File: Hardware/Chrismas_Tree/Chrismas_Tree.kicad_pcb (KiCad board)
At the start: 2 copper layers, 144 parts

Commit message: Added tree trunk to schematic and PCB.
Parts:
- added D73: LED, LED_THT:LED_D5.0mm, F.Cu at (185.7, 325.6)
- added D74: LED, LED_THT:LED_D5.0mm, F.Cu at (136.7, 325.6)
- added D75: LED, LED_THT:LED_D5.0mm, F.Cu at (185.7, 337.6)
- added D76: LED, LED_THT:LED_D5.0mm, F.Cu at (136.7, 337.6)
- added D77: LED, LED_THT:LED_D5.0mm, F.Cu at (185.7, 348.7)
- added D78: LED, LED_THT:LED_D5.0mm, F.Cu at (136.7, 348.7)
- added D79: LED, LED_THT:LED_D5.0mm, F.Cu at (172.7, 350.0)
- added D80: LED, LED_THT:LED_D5.0mm, F.Cu at (149.9, 350.0)
- added D81: LED, LED_THT:LED_D5.0mm, F.Cu at (161.0, 350.0)
- added R73: R, Resistor_THT:R_Axial_DIN0207_L6.3mm_D2.5mm_P7.62mm_Horizontal, F.Cu at (429.0, 207.3)
- added R74: R, Resistor_THT:R_Axial_DIN0207_L6.3mm_D2.5mm_P7.62mm_Horizontal, F.Cu at (429.0, 211.4)
- added R75: R, Resistor_THT:R_Axial_DIN0207_L6.3mm_D2.5mm_P7.62mm_Horizontal, F.Cu at (439.8, 207.3)
- added R76: R, Resistor_THT:R_Axial_DIN0207_L6.3mm_D2.5mm_P7.62mm_Horizontal, F.Cu at (429.0, 215.4)
- added R77: R, Resistor_THT:R_Axial_DIN0207_L6.3mm_D2.5mm_P7.62mm_Horizontal, F.Cu at (439.8, 211.4)
- added R78: R, Resistor_THT:R_Axial_DIN0207_L6.3mm_D2.5mm_P7.62mm_Horizontal, F.Cu at (429.0, 219.5)
- added R79: R, Resistor_THT:R_Axial_DIN0207_L6.3mm_D2.5mm_P7.62mm_Horizontal, F.Cu at (450.6, 207.3)
- added R80: R, Resistor_THT:R_Axial_DIN0207_L6.3mm_D2.5mm_P7.62mm_Horizontal, F.Cu at (429.0, 223.5)
- added R81: R, Resistor_THT:R_Axial_DIN0207_L6.3mm_D2.5mm_P7.62mm_Horizontal, F.Cu at (146.3, 384.3)
- moved D72 323.7 mm to (136.7, 314.2)
- moved D70 311.0 mm to (136.7, 302.8)
- moved D71 293.3 mm to (185.7, 314.2), turned to 180 degrees
- moved D69 259.4 mm to (185.7, 302.8), turned to 180 degrees
- moved D67 2.54 mm to (177.0, 290.3), turned to 180 degrees
- moved D63 2.54 mm to (209.8, 286.8), turned to 180 degrees
- moved D65 2.54 mm to (193.0, 289.8), turned to 180 degrees
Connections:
- D69 pad 1: GND -> Net-(D69-Pad1)
- D70 pad 1: GND -> Net-(D69-Pad1)
- D71 pad 1: GND -> Net-(D69-Pad1)
- D72 pad 1: GND -> Net-(D69-Pad1)
- R69 pad 1: Net-(R1-Pad1) -> Net-(R69-Pad1)
- R70 pad 1: Net-(R1-Pad1) -> Net-(R70-Pad1)
- R71 pad 1: Net-(R1-Pad1) -> Net-(R71-Pad1)
- R72 pad 1: Net-(R1-Pad1) -> Net-(R72-Pad1)

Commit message: Reorganized schematic to use several sheets.
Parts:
- added D82: LED, LED_THT:LED_D5.0mm, F.Cu at (115.1, 92.7)
- added D83: LED, LED_THT:LED_D5.0mm, F.Cu at (204.0, 95.0)
- added D84: LED, LED_THT:LED_D5.0mm, F.Cu at (91.7, 154.2)
- added D85: LED, LED_THT:LED_D5.0mm, F.Cu at (227.1, 157.0)
- added D86: LED, LED_THT:LED_D5.0mm, F.Cu at (77.0, 216.2)
- added D87: LED, LED_THT:LED_D5.0mm, F.Cu at (238.5, 217.4)
- added D88: LED, LED_THT:LED_D5.0mm, F.Cu at (51.3, 289.1)
- added D89: LED, LED_THT:LED_D5.0mm, F.Cu at (262.4, 286.0)
- added D90: LED, LED_THT:LED_D5.0mm, F.Cu at (90.9, 299.2)
- added D91: LED, LED_THT:LED_D5.0mm, F.Cu at (220.7, 296.2)
- added D92: LED, LED_THT:LED_D5.0mm, F.Cu at (156.2, 8.89)
- added D93: LED, LED_THT:LED_D5.0mm, F.Cu at (164.3, 8.89)
- added D94: LED, LED_THT:LED_D5.0mm, F.Cu at (160.3, 18.3)
- added D95: LED, LED_THT:LED_D5.0mm, F.Cu at (160.5, 0.00)
- added R82: R, Resistor_THT:R_Axial_DIN0207_L6.3mm_D2.5mm_P7.62mm_Horizontal, F.Cu at (352.6, 261.0)
- added R83: R, Resistor_THT:R_Axial_DIN0207_L6.3mm_D2.5mm_P7.62mm_Horizontal, F.Cu at (363.3, 257.0)
- added R84: R, Resistor_THT:R_Axial_DIN0207_L6.3mm_D2.5mm_P7.62mm_Horizontal, F.Cu at (352.6, 265.1)
- added R85: R, Resistor_THT:R_Axial_DIN0207_L6.3mm_D2.5mm_P7.62mm_Horizontal, F.Cu at (363.3, 261.0)
- added R86: R, Resistor_THT:R_Axial_DIN0207_L6.3mm_D2.5mm_P7.62mm_Horizontal, F.Cu at (352.6, 269.1)
- added R87: R, Resistor_THT:R_Axial_DIN0207_L6.3mm_D2.5mm_P7.62mm_Horizontal, F.Cu at (374.1, 257.0)
- added R88: R, Resistor_THT:R_Axial_DIN0207_L6.3mm_D2.5mm_P7.62mm_Horizontal, F.Cu at (352.6, 273.2)
- added R89: R, Resistor_THT:R_Axial_DIN0207_L6.3mm_D2.5mm_P7.62mm_Horizontal, F.Cu at (363.3, 265.1)
- added R90: R, Resistor_THT:R_Axial_DIN0207_L6.3mm_D2.5mm_P7.62mm_Horizontal, F.Cu at (374.1, 261.0)
- added R91: R, Resistor_THT:R_Axial_DIN0207_L6.3mm_D2.5mm_P7.62mm_Horizontal, F.Cu at (363.3, 269.1)
- added R92: R, Resistor_THT:R_Axial_DIN0207_L6.3mm_D2.5mm_P7.62mm_Horizontal, F.Cu at (352.6, 277.2)
- added R93: R, Resistor_THT:R_Axial_DIN0207_L6.3mm_D2.5mm_P7.62mm_Horizontal, F.Cu at (352.6, 281.3)
- added R94: R, Resistor_THT:R_Axial_DIN0207_L6.3mm_D2.5mm_P7.62mm_Horizontal, F.Cu at (352.6, 257.0)
- added R95: R, Resistor_THT:R_Axial_DIN0207_L6.3mm_D2.5mm_P7.62mm_Horizontal, F.Cu at (410.5, 24.2)
- moved R1 122.3 mm to (294.9, -25.1)
- moved R10 122.3 mm to (325.3, -16.0)
- moved R12 122.3 mm to (294.9, -4.90)
- moved R15 122.3 mm to (325.3, -12.0)
- moved R17 122.3 mm to (325.3, -7.92)
- moved R19 122.3 mm to (325.3, -3.87)
- moved R2 122.3 mm to (294.9, -21.1)
- moved R20 122.3 mm to (325.3, 0.18)
- moved R4 122.3 mm to (294.9, -17.0)
- moved R6 122.3 mm to (294.9, -13.0)
- moved R7 122.3 mm to (325.3, -20.1)
- moved R8 122.3 mm to (294.9, -8.95)
- moved R11 122.3 mm to (314.6, -7.92)
- moved R13 122.3 mm to (336.1, -20.1)
- moved R14 122.3 mm to (314.6, -3.87)
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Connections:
- D69 pad 1: Net-(D69-Pad1) -> GND
- D70 pad 1: Net-(D69-Pad1) -> GND
- D71 pad 1: Net-(D69-Pad1) -> GND
- D72 pad 1: Net-(D69-Pad1) -> GND
- D73 pad 1: Net-(D73-Pad1) -> GND
- D74 pad 1: Net-(D73-Pad1) -> GND
- D75 pad 1: Net-(D73-Pad1) -> GND
- D76 pad 1: Net-(D73-Pad1) -> GND
- D77 pad 1: Net-(D77-Pad1) -> GND
- D78 pad 1: Net-(D77-Pad1) -> GND
- D79 pad 1: Net-(D77-Pad1) -> GND
- D80 pad 1: Net-(D77-Pad1) -> GND
- D81 pad 1: Net-(D77-Pad1) -> GND
- R1 pad 1: Net-(R1-Pad1) -> +5V
- R10 pad 1: Net-(R1-Pad1) -> +5V
- R11 pad 1: Net-(R1-Pad1) -> +5V
- R12 pad 1: Net-(R1-Pad1) -> +5V
- R13 pad 1: Net-(R1-Pad1) -> +5V
- R14 pad 1: Net-(R1-Pad1) -> +5V
- R15 pad 1: Net-(R1-Pad1) -> +5V
- R16 pad 1: Net-(R1-Pad1) -> +5V
- R17 pad 1: Net-(R1-Pad1) -> +5V
- R18 pad 1: Net-(R1-Pad1) -> +5V
- R19 pad 1: Net-(R1-Pad1) -> +5V
- R2 pad 1: Net-(R1-Pad1) -> +5V
- R20 pad 1: Net-(R1-Pad1) -> +5V
- R21 pad 1: Net-(R1-Pad1) -> +5V
- R22 pad 1: Net-(R1-Pad1) -> +5V
- R23 pad 1: Net-(R1-Pad1) -> +5V
- R24 pad 1: Net-(R1-Pad1) -> +5V
- R25 pad 1: Net-(R1-Pad1) -> +5V
- R26 pad 1: Net-(R1-Pad1) -> +5V
- R27 pad 1: Net-(R1-Pad1) -> +5V
- R28 pad 1: Net-(R1-Pad1) -> +5V
- R29 pad 1: Net-(R1-Pad1) -> +5V
- R3 pad 1: Net-(R1-Pad1) -> +5V
- R30 pad 1: Net-(R1-Pad1) -> +5V
- R31 pad 1: Net-(R1-Pad1) -> +5V
- R32 pad 1: Net-(R1-Pad1) -> +5V
- R33 pad 1: Net-(R1-Pad1) -> +5V
- R34 pad 1: Net-(R1-Pad1) -> +5V
- R35 pad 1: Net-(R1-Pad1) -> +5V
- R36 pad 1: Net-(R1-Pad1) -> +5V
- R37 pad 1: Net-(R1-Pad1) -> +5V
- R38 pad 1: Net-(R1-Pad1) -> +5V
- R39 pad 1: Net-(R1-Pad1) -> +5V
- R4 pad 1: Net-(R1-Pad1) -> +5V
- R40 pad 1: Net-(R1-Pad1) -> +5V
- R41 pad 1: Net-(R1-Pad1) -> +5V
- R42 pad 1: Net-(R1-Pad1) -> +5V
- R43 pad 1: Net-(R1-Pad1) -> +5V
- R44 pad 1: Net-(R1-Pad1) -> +5V
- R45 pad 1: Net-(R1-Pad1) -> +5V
- R46 pad 1: Net-(R1-Pad1) -> +5V
- R47 pad 1: Net-(R1-Pad1) -> +5V
- R48 pad 1: Net-(R1-Pad1) -> +5V
- R49 pad 1: Net-(R1-Pad1) -> +5V
- R5 pad 1: Net-(R1-Pad1) -> +5V
- R50 pad 1: Net-(R1-Pad1) -> +5V
- R51 pad 1: Net-(R1-Pad1) -> +5V
- R52 pad 1: Net-(R1-Pad1) -> +5V
- R53 pad 1: Net-(R1-Pad1) -> +5V
- R54 pad 1: Net-(R1-Pad1) -> +5V
- R55 pad 1: Net-(R1-Pad1) -> +5V
- R56 pad 1: Net-(R1-Pad1) -> +5V
- R57 pad 1: Net-(R1-Pad1) -> +5V
- R58 pad 1: Net-(R1-Pad1) -> +5V
- R59 pad 1: Net-(R1-Pad1) -> +5V
- R6 pad 1: Net-(R1-Pad1) -> +5V
- R60 pad 1: Net-(R1-Pad1) -> +5V
- R61 pad 1: Net-(R1-Pad1) -> +5V
- R62 pad 1: Net-(R1-Pad1) -> +5V
- R63 pad 1: Net-(R1-Pad1) -> +5V
- R64 pad 1: Net-(R1-Pad1) -> +5V
- R65 pad 1: Net-(R1-Pad1) -> +5V
- R66 pad 1: Net-(R1-Pad1) -> +5V
- R67 pad 1: Net-(R1-Pad1) -> +5V
- R68 pad 1: Net-(R1-Pad1) -> +5V
- R69 pad 1: Net-(R69-Pad1) -> +5V
- R7 pad 1: Net-(R1-Pad1) -> +5V
- R70 pad 1: Net-(R70-Pad1) -> +5V
- R71 pad 1: Net-(R71-Pad1) -> +5V
- R72 pad 1: Net-(R72-Pad1) -> +5V
- R73 pad 1: Net-(R73-Pad1) -> +5V
- R74 pad 1: Net-(R74-Pad1) -> +5V
- R75 pad 1: Net-(R75-Pad1) -> +5V
- R76 pad 1: Net-(R76-Pad1) -> +5V
- R77 pad 1: Net-(R77-Pad1) -> +5V
- R78 pad 1: Net-(R78-Pad1) -> +5V
- R79 pad 1: Net-(R79-Pad1) -> +5V
- R8 pad 1: Net-(R1-Pad1) -> +5V
- R80 pad 1: Net-(R80-Pad1) -> +5V
- R81 pad 1: Net-(R81-Pad1) -> +5V
- R9 pad 1: Net-(R1-Pad1) -> +5V

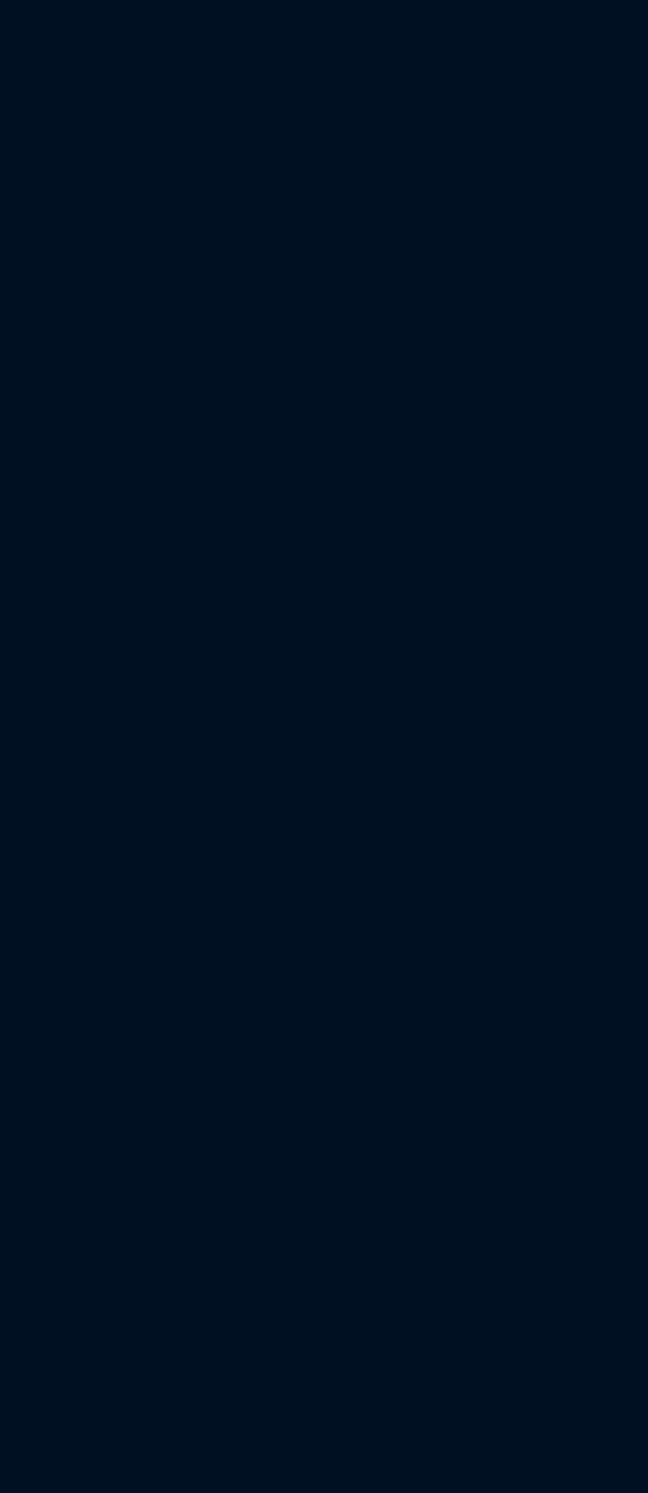
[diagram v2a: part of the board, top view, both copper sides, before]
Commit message: Added microcontroller symbol and footprint.
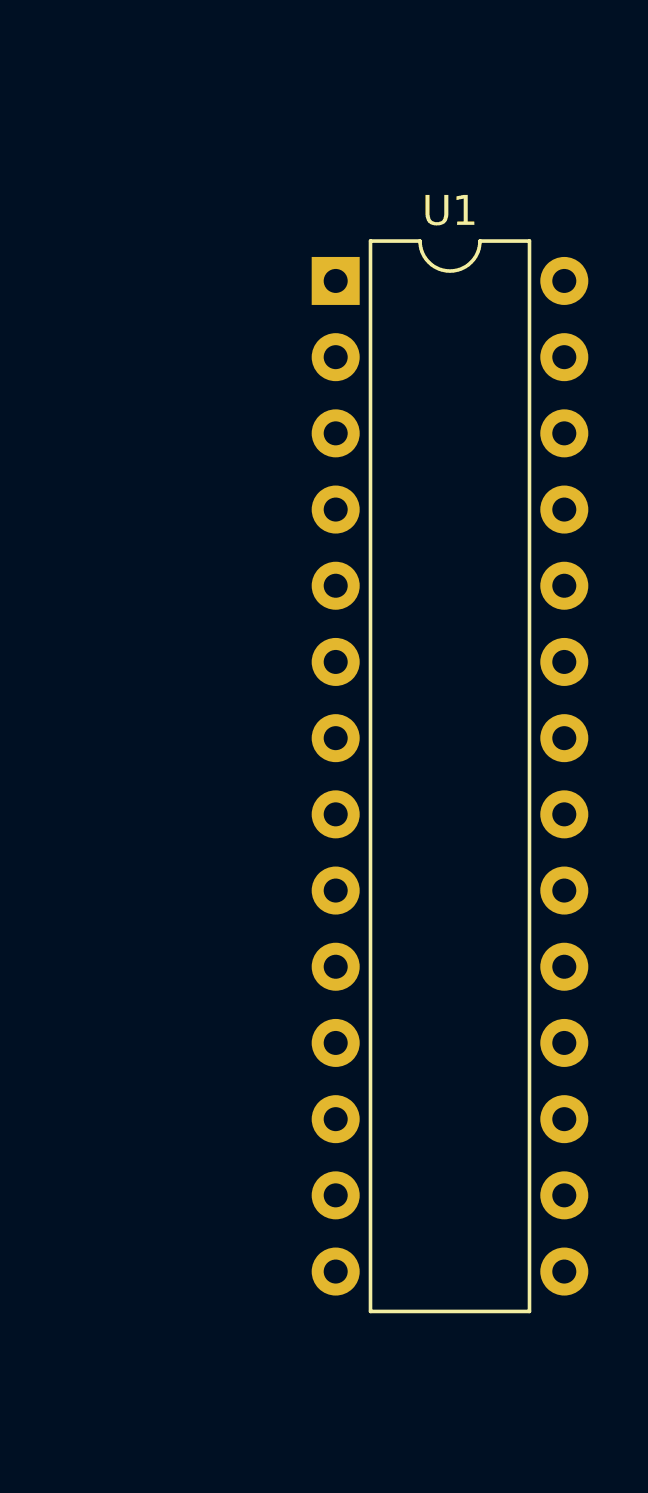
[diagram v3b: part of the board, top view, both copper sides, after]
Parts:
- added U1: PIC18F23K22, Package_DIP:DIP-28_W7.62mm, F.Cu at (458.5, 160.5)
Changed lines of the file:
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@@
     (tracks 0)
     (zones 0)
-    (modules 190)
-    (nets 99)
+    (modules 191)
+    (nets 127)
   )
   (page A4)
@@
   (net 97 "Net-(R82-Pad1)")
   (net 98 "Net-(D95-Pad2)")
+  (net 99 "Net-(U1-Pad28)")
+  (net 100 "Net-(U1-Pad14)")
+  (net 101 "Net-(U1-Pad27)")
+  (net 102 "Net-(U1-Pad13)")
+  (net 103 "Net-(U1-Pad26)")
+  (net 104 "Net-(U1-Pad12)")
+  (net 105 "Net-(U1-Pad25)")
+  (net 106 "Net-(U1-Pad11)")
+  (net 107 "Net-(U1-Pad24)")
+  (net 108 "Net-(U1-Pad10)")
+  (net 109 "Net-(U1-Pad23)")
+  (net 110 "Net-(U1-Pad9)")
+  (net 111 "Net-(U1-Pad22)")
+  (net 112 "Net-(U1-Pad8)")
+  (net 113 "Net-(U1-Pad21)")
+  (net 114 "Net-(U1-Pad7)")
+  (net 115 "Net-(U1-Pad20)")
+  (net 116 "Net-(U1-Pad6)")
+  (net 117 "Net-(U1-Pad19)")
+  (net 118 "Net-(U1-Pad5)")
+  (net 119 "Net-(U1-Pad18)")
+  (net 120 "Net-(U1-Pad4)")
+  (net 121 "Net-(U1-Pad17)")
+  (net 122 "Net-(U1-Pad3)")
+  (net 123 "Net-(U1-Pad16)")
+  (net 124 "Net-(U1-Pad2)")
+  (net 125 "Net-(U1-Pad15)")
+  (net 126 "Net-(U1-Pad1)")
   (net_class Default "Ceci est la Netclass par défaut."
     (clearance 0.2)
@@
     (add_net "Net-(D95-Pad2)")
     (add_net "Net-(R82-Pad1)")
+    (add_net "Net-(U1-Pad1)")
+    (add_net "Net-(U1-Pad10)")
+    (add_net "Net-(U1-Pad11)")
+    (add_net "Net-(U1-Pad12)")
+    (add_net "Net-(U1-Pad13)")
+    (add_net "Net-(U1-Pad14)")
+    (add_net "Net-(U1-Pad15)")
+    (add_net "Net-(U1-Pad16)")
+    (add_net "Net-(U1-Pad17)")
+    (add_net "Net-(U1-Pad18)")
+    (add_net "Net-(U1-Pad19)")
+    (add_net "Net-(U1-Pad2)")
+    (add_net "Net-(U1-Pad20)")
+    (add_net "Net-(U1-Pad21)")
+    (add_net "Net-(U1-Pad22)")
+    (add_net "Net-(U1-Pad23)")
+    (add_net "Net-(U1-Pad24)")
+    (add_net "Net-(U1-Pad25)")
+    (add_net "Net-(U1-Pad26)")
+    (add_net "Net-(U1-Pad27)")
+    (add_net "Net-(U1-Pad28)")
+    (add_net "Net-(U1-Pad3)")
+    (add_net "Net-(U1-Pad4)")
+    (add_net "Net-(U1-Pad5)")
+    (add_net "Net-(U1-Pad6)")
+    (add_net "Net-(U1-Pad7)")
+    (add_net "Net-(U1-Pad8)")
+    (add_net "Net-(U1-Pad9)")
+  )
+  (module Package_DIP:DIP-28_W7.62mm (layer F.Cu)
+    (at 458.47 160.528)
+    (descr "28-lead though-hole mounted DIP package, row spacing 7.62 mm (300 mils)")
+    (tags "THT DIP DIL PDIP 2.54mm 7.62mm 300mil")
+    (fp_text reference U1 (at 3.81 -2.33) (layer F.SilkS)
+      (effects (font (size 1 1) (thickness 0.15)))
+    )
+    (fp_text value PIC18F23K22 (at 3.81 35.35) (layer F.Fab)
+      (effects (font (size 1 1) (thickness 0.15)))
+    )
+    (fp_text user %R (at 3.81 16.51) (layer F.Fab)
+      (effects (font (size 1 1) (thickness 0.15)))
+    )
+    (fp_line (start 8.7 -1.55) (end -1.1 -1.55) (layer F.CrtYd) (width 0.05))
+    (fp_line (start 8.7 34.55) (end 8.7 -1.55) (layer F.CrtYd) (width 0.05))
+    (fp_line (start -1.1 34.55) (end 8.7 34.55) (layer F.CrtYd) (width 0.05))
+    (fp_line (start -1.1 -1.55) (end -1.1 34.55) (layer F.CrtYd) (width 0.05))
+    (fp_line (start 6.46 -1.33) (end 4.81 -1.33) (layer F.SilkS) (width 0.12))
+    (fp_line (start 6.46 34.35) (end 6.46 -1.33) (layer F.SilkS) (width 0.12))
+    (fp_line (start 1.16 34.35) (end 6.46 34.35) (layer F.SilkS) (width 0.12))
+    (fp_line (start 1.16 -1.33) (end 1.16 34.35) (layer F.SilkS) (width 0.12))
+    (fp_line (start 2.81 -1.33) (end 1.16 -1.33) (layer F.SilkS) (width 0.12))
+    (fp_line (start 0.635 -0.27) (end 1.635 -1.27) (layer F.Fab) (width 0.1))
+    (fp_line (start 0.635 34.29) (end 0.635 -0.27) (layer F.Fab) (width 0.1))
+    (fp_line (start 6.985 34.29) (end 0.635 34.29) (layer F.Fab) (width 0.1))
+    (fp_line (start 6.985 -1.27) (end 6.985 34.29) (layer F.Fab) (width 0.1))
+    (fp_line (start 1.635 -1.27) (end 6.985 -1.27) (layer F.Fab) (width 0.1))
+    (fp_arc (start 3.81 -1.33) (end 2.81 -1.33) (angle -180) (layer F.SilkS) (width 0.12))
+    (pad 28 thru_hole oval (at 7.62 0) (size 1.6 1.6) (drill 0.8) (layers *.Cu *.Mask)
+      (net 99 "Net-(U1-Pad28)"))
+    (pad 14 thru_hole oval (at 0 33.02) (size 1.6 1.6) (drill 0.8) (layers *.Cu *.Mask)
+      (net 100 "Net-(U1-Pad14)"))
+    (pad 27 thru_hole oval (at 7.62 2.54) (size 1.6 1.6) (drill 0.8) (layers *.Cu *.Mask)
+      (net 101 "Net-(U1-Pad27)"))
+    (pad 13 thru_hole oval (at 0 30.48) (size 1.6 1.6) (drill 0.8) (layers *.Cu *.Mask)
+      (net 102 "Net-(U1-Pad13)"))
+    (pad 26 thru_hole oval (at 7.62 5.08) (size 1.6 1.6) (drill 0.8) (layers *.Cu *.Mask)
+      (net 103 "Net-(U1-Pad26)"))
+    (pad 12 thru_hole oval (at 0 27.94) (size 1.6 1.6) (drill 0.8) (layers *.Cu *.Mask)
+      (net 104 "Net-(U1-Pad12)"))
+    (pad 25 thru_hole oval (at 7.62 7.62) (size 1.6 1.6) (drill 0.8) (layers *.Cu *.Mask)
+      (net 105 "Net-(U1-Pad25)"))
+    (pad 11 thru_hole oval (at 0 25.4) (size 1.6 1.6) (drill 0.8) (layers *.Cu *.Mask)
+      (net 106 "Net-(U1-Pad11)"))
+    (pad 24 thru_hole oval (at 7.62 10.16) (size 1.6 1.6) (drill 0.8) (layers *.Cu *.Mask)
+      (net 107 "Net-(U1-Pad24)"))
+    (pad 10 thru_hole oval (at 0 22.86) (size 1.6 1.6) (drill 0.8) (layers *.Cu *.Mask)
+      (net 108 "Net-(U1-Pad10)"))
+    (pad 23 thru_hole oval (at 7.62 12.7) (size 1.6 1.6) (drill 0.8) (layers *.Cu *.Mask)
+      (net 109 "Net-(U1-Pad23)"))
+    (pad 9 thru_hole oval (at 0 20.32) (size 1.6 1.6) (drill 0.8) (layers *.Cu *.Mask)
+      (net 110 "Net-(U1-Pad9)"))
+    (pad 22 thru_hole oval (at 7.62 15.24) (size 1.6 1.6) (drill 0.8) (layers *.Cu *.Mask)
+      (net 111 "Net-(U1-Pad22)"))
+    (pad 8 thru_hole oval (at 0 17.78) (size 1.6 1.6) (drill 0.8) (layers *.Cu *.Mask)
+      (net 112 "Net-(U1-Pad8)"))
+    (pad 21 thru_hole oval (at 7.62 17.78) (size 1.6 1.6) (drill 0.8) (layers *.Cu *.Mask)
+      (net 113 "Net-(U1-Pad21)"))
+    (pad 7 thru_hole oval (at 0 15.24) (size 1.6 1.6) (drill 0.8) (layers *.Cu *.Mask)
+      (net 114 "Net-(U1-Pad7)"))
+    (pad 20 thru_hole oval (at 7.62 20.32) (size 1.6 1.6) (drill 0.8) (layers *.Cu *.Mask)
+      (net 115 "Net-(U1-Pad20)"))
+    (pad 6 thru_hole oval (at 0 12.7) (size 1.6 1.6) (drill 0.8) (layers *.Cu *.Mask)
+      (net 116 "Net-(U1-Pad6)"))
+    (pad 19 thru_hole oval (at 7.62 22.86) (size 1.6 1.6) (drill 0.8) (layers *.Cu *.Mask)
+      (net 117 "Net-(U1-Pad19)"))
+    (pad 5 thru_hole oval (at 0 10.16) (size 1.6 1.6) (drill 0.8) (layers *.Cu *.Mask)
+      (net 118 "Net-(U1-Pad5)"))
+    (pad 18 thru_hole oval (at 7.62 25.4) (size 1.6 1.6) (drill 0.8) (layers *.Cu *.Mask)
+      (net 119 "Net-(U1-Pad18)"))
+    (pad 4 thru_hole oval (at 0 7.62) (size 1.6 1.6) (drill 0.8) (layers *.Cu *.Mask)
+      (net 120 "Net-(U1-Pad4)"))
+    (pad 17 thru_hole oval (at 7.62 27.94) (size 1.6 1.6) (drill 0.8) (layers *.Cu *.Mask)
+      (net 121 "Net-(U1-Pad17)"))
+    (pad 3 thru_hole oval (at 0 5.08) (size 1.6 1.6) (drill 0.8) (layers *.Cu *.Mask)
+      (net 122 "Net-(U1-Pad3)"))
+    (pad 16 thru_hole oval (at 7.62 30.48) (size 1.6 1.6) (drill 0.8) (layers *.Cu *.Mask)
+      (net 123 "Net-(U1-Pad16)"))
+    (pad 2 thru_hole oval (at 0 2.54) (size 1.6 1.6) (drill 0.8) (layers *.Cu *.Mask)
+      (net 124 "Net-(U1-Pad2)"))
+    (pad 15 thru_hole oval (at 7.62 33.02) (size 1.6 1.6) (drill 0.8) (layers *.Cu *.Mask)
+      (net 125 "Net-(U1-Pad15)"))
+    (pad 1 thru_hole rect (at 0 0) (size 1.6 1.6) (drill 0.8) (layers *.Cu *.Mask)
+      (net 126 "Net-(U1-Pad1)"))
+    (model ${KISYS3DMOD}/Package_DIP.3dshapes/DIP-28_W7.62mm.wrl
+      (at (xyz 0 0 0))
+      (scale (xyz 1 1 1))
+      (rotate (xyz 0 0 0))
+    )
   )
   (module Resistor_THT:R_Axial_DIN0207_L6.3mm_D2.5mm_P7.62mm_Horizontal (layer F.Cu)

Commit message: Placed all tree foliage and trunk resistors on the PCB.
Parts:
- R1, R10, R11, R12, R13, R14, R15, R16, R17, R18, R19, R2, R20, R21, R22, R23, R24, R25, R26, R27, R28, R29, R3, R30, R31, R32, R33, R34, R35, R36, R37, R38, R39, R4, R40, R41, R42, R43, R44, R45, R46, R47, R48, R49, R5, R50, R51, R52, R53, R54, R55, R56, R57, R58, R59, R6, R60, R61, R62, R63, R64, R65, R66, R67, R68, R69, R7, R70, R71, R72, R73, R74, R75, R76, R77, R78, R79, R8, R80, R81, R9: moved to B.Cu
- moved R58 358.7 mm to (81.3, 271.8), turned to 270 degrees
- moved R54 357.7 mm to (52.1, 262.9), turned to 180 degrees
- moved R52 349.2 mm to (62.2, 261.6), turned to 90 degrees
- moved R60 334.6 mm to (99.1, 275.6), turned to 270 degrees
- moved R56 322.2 mm to (62.2, 266.7), turned to 270 degrees
- moved R79 311.0 mm to (167.6, 336.6), turned to 270 degrees
- moved R76 305.4 mm to (146.1, 330.2), turned to 270 degrees
- moved R50 305.3 mm to (87.6, 251.5), turned to 180 degrees
- moved R78 305.2 mm to (149.9, 342.9), turned to 180 degrees
- moved R74 299.1 mm to (152.4, 325.1), turned to 180 degrees
- moved R77 297.7 mm to (172.7, 342.9)
- moved R80 296.5 mm to (154.9, 336.6), turned to 270 degrees
- moved R75 293.8 mm to (176.5, 337.8), turned to 90 degrees
- moved R72 293.1 mm to (152.4, 313.7), turned to 180 degrees
- moved R73 284.4 mm to (170.2, 325.1)
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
